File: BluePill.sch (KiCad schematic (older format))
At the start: 68 parts

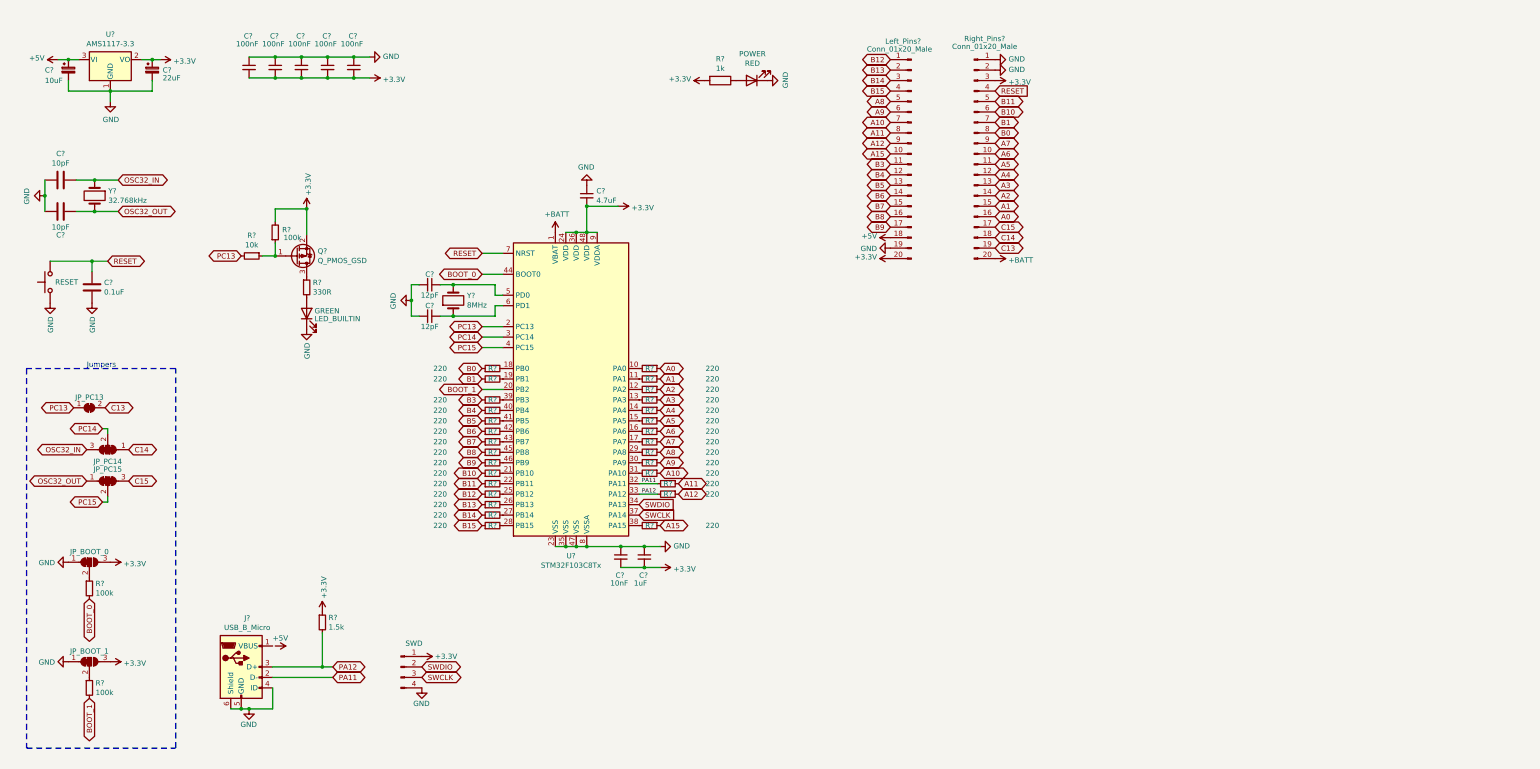
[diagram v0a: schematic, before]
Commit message: Finish schematic
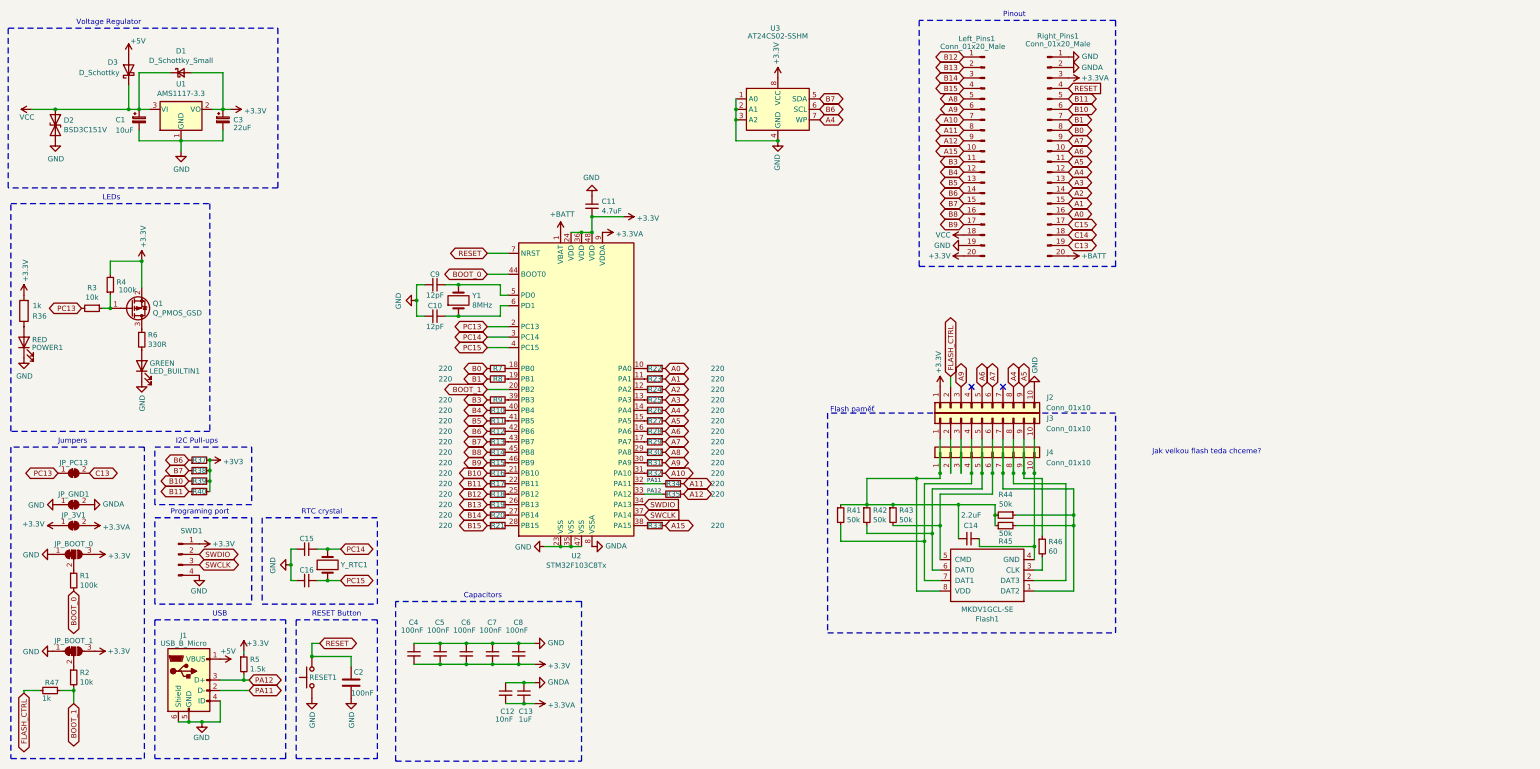
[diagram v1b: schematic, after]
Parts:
- removed C? (x2): 10pF, symbol Device:C
- removed JP_PC14, JP_PC15: SolderJumper_3_Bridged123, symbol Jumper:SolderJumper_3_Bridged123
- removed Y?: 32.768kHz, symbol Device:Crystal
- added C14: 2.2uF, Capacitor_SMD:C_0402_1005Metric, symbol Device:C_Small
- added C15, C16: ?, Capacitor_SMD:C_0603_1608Metric_Pad1.08x0.95mm_HandSolder, symbol Device:C_Small
- added D1: D_Schottky_Small, BluePill:DFN-2L_L1.0-W0.6-P0.65-RD, symbol Device:D_Schottky_Small
- added D2: BSD3C151V, Diode_SMD:D_SOD-323, symbol Device:D_TVS
- added D3: D_Schottky, Diode_SMD:D_SOD-323F, symbol Device:D_Schottky
- added Flash1: MKDV1GCL-SE, BluePill:LGA-8_L6.0-W8.0-P1.27-TL, symbol LGA-8_L6.0-W8.0-P1.27-TL:LGA-8_L6.0-W8.0-P1.27-TL
- added J2, J3, J4: Conn_01x10, symbol Connector_Generic:Conn_01x10
- added JP_3V1: 3V3, Jumper:SolderJumper-2_P1.3mm_Bridged_RoundedPad1.0x1.5mm, symbol Jumper:SolderJumper_2_Bridged
- added JP_GND1: GND, Jumper:SolderJumper-2_P1.3mm_Bridged_RoundedPad1.0x1.5mm, symbol Jumper:SolderJumper_2_Bridged
- added R37, R38, R39, R40: ?, Resistor_SMD:R_0603_1608Metric_Pad0.98x0.95mm_HandSolder, symbol Device:R_Small
- added R41, R42, R43, R44, R45: 50k, Resistor_SMD:R_0402_1005Metric, symbol Device:R_Small
- added R46: 60, Resistor_SMD:R_0402_1005Metric, symbol Device:R_Small
- added R47: 1k, Resistor_SMD:R_0402_1005Metric, symbol Device:R_Small
- added U3: AT24CS02-SSHM, Package_SO:SOIC-8_3.9x4.9mm_P1.27mm, symbol Memory_EEPROM:AT24CS02-SSHM
- added Y_RTC1: ?, Crystal:Crystal_SMD_5032-2Pin_5.0x3.2mm_HandSoldering, symbol Device:Crystal
- C1: renamed from C?; footprint (none) -> Capacitor_Tantalum_SMD:CP_EIA-3216-18_Kemet-A; LCSC (none) -> C117023
- C10, C12, C4, C5, C6, C7, C8, C9: renamed from C?; footprint (none) -> Capacitor_SMD:C_0402_1005Metric
- C11: renamed from C?; footprint (none) -> Capacitor_SMD:C_0402_1005Metric; LCSC (none) -> C23733; Note (none) -> This has to be connected near the same pin as in datasheet!
- C13: renamed from C?; footprint (none) -> Capacitor_SMD:C_0402_1005Metric; LCSC (none) -> C52923
- C2: renamed from C?; value 0.1uF -> 100nF; footprint (none) -> Capacitor_SMD:C_0402_1005Metric
- C3: renamed from C?; footprint (none) -> Capacitor_Tantalum_SMD:CP_EIA-2012-15_AVX-P; LCSC (none) -> C11383
- J1: renamed from J?; footprint (none) -> BluePill:MICRO-USB-SMD_MICRO-USB-A11; LCSC (none) -> C145783
- JP_BOOT_0, JP_BOOT_1: footprint (none) -> Jumper:SolderJumper-3_P1.3mm_Bridged12_RoundedPad1.0x1.5mm
- JP_PC13: footprint (none) -> Jumper:SolderJumper-2_P1.3mm_Bridged_RoundedPad1.0x1.5mm
- Left_Pins1: renamed from Left_Pins?; footprint (none) -> Connector_PinHeader_2.54mm:PinHeader_1x20_P2.54mm_Vertical
- Q1: renamed from Q?; footprint (none) -> BluePill:VBTA2245M; LCSC (none) -> C692958
- R1, R10, R11, R12, R13, R14, R15, R16, R17, R18, R19, R20, R21, R22, R23, R24, R25, R26, R27, R28, R29, R3, R30, R31, R32, R33, R34, R35, R36, R4, R5, R6, R7, R8, R9: renamed from R?; footprint (none) -> Resistor_SMD:R_0402_1005Metric
- R2: renamed from R?; value 100k -> 10k; footprint (none) -> Resistor_SMD:R_0402_1005Metric
- RESET1: renamed from RESET; footprint (none) -> BluePill:KEY-SMD_B3U-1000PM; LCSC (none) -> C231329
- Right_Pins1: renamed from Right_Pins?; footprint (none) -> Connector_PinHeader_2.54mm:PinHeader_1x20_P2.54mm_Vertical
- SWD1: renamed from SWD; footprint (none) -> Connector_PinHeader_2.54mm:PinHeader_1x04_P2.54mm_Vertical
- Y1: renamed from Y?; footprint (none) -> BluePill:OSC-SMD_L5.0-W3.2
- gave numbers to parts that had none: 2
- renumbered LED_BUILTIN to LED_BUILTIN1, POWER to POWER1
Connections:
- net +3V3: now also D1.2 (A), J2.1 (Pin_1), JP_3V1.1 (A), R37.2, R38.2, R39.2, R40.2, U3.8 (VCC); no longer C12.2, C13.2, Right_Pins1.3 (Pin_3), U2.9 (VDDA)
- net +5V: now also J1.1 (VBUS), D3.2 (A); no longer C1.1, Left_Pins1.18 (Pin_18), U1.3 (VI)
- net A4: now also J2.8 (Pin_8), U3.7 (WP)
- net A5: now also J2.9 (Pin_9)
- net A6: now also J2.5 (Pin_5)
- net A7: now also J2.6 (Pin_6)
- net A9: now also J2.3 (Pin_3)
- net B10: now also R39.1
- net B11: now also R40.1
- net B6: now also R37.1, U3.6 (SCL)
- net B7: now also R38.1, U3.5 (SDA)
- net BOOT_1: now also R47.1
- net GND: now also C15.2, C16.2, D2.2 (A2), J2.10 (Pin_10), JP_GND1.1 (A), U3.1 (A0), U3.2 (A1), U3.3 (A2), U3.4 (GND); no longer C12.1, C13.1, Right_Pins1.2 (Pin_2), U2.8 (VSSA)
- net PC14: now also C15.1, Y_RTC1.2
- net PC15: now also C16.1, Y_RTC1.1
- new net: C14.2, Flash1.8 (VDD), J3.1 (Pin_1), J4.1 (Pin_1), R41.1, R42.1, R43.1, R44.2, R45.1
- new net: C14.1, Flash1.4 (GND), J3.10 (Pin_10), J4.10 (Pin_10)
- new net: J3.2 (Pin_2), J4.2 (Pin_2)
- new net: J3.3 (Pin_3), J4.3 (Pin_3)
- new net: Flash1.7 (DAT1), J3.4 (Pin_4), J4.4 (Pin_4), R41.2
- new net: Flash1.6 (DAT0), J3.5 (Pin_5), J4.5 (Pin_5), R42.2
- new net: Flash1.5 (CMD), J3.6 (Pin_6), J4.6 (Pin_6), R43.2
- new net: Flash1.1 (DAT2), J3.7 (Pin_7), J4.7 (Pin_7), R44.1, R45.2
- new net: Flash1.2 (DAT3), J3.8 (Pin_8), J4.8 (Pin_8)
- new net: J3.9 (Pin_9), J4.9 (Pin_9), R46.1
- new net: Flash1.3 (CLK), R46.2
- new net +3.3VA: C12.2, C13.2, JP_3V1.2 (B), Right_Pins1.3 (Pin_3), U2.9 (VDDA)
- new net FLASH_CTRL: J2.2 (Pin_2), R47.2
- new net GNDA: C12.1, C13.1, JP_GND1.2 (B), Right_Pins1.2 (Pin_2), U2.8 (VSSA)
- new net VCC: C1.1, D1.1 (K), D2.1 (A1), D3.1 (K), Left_Pins1.18 (Pin_18), U1.3 (VI)
- no-connect marks 0 -> 2
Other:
- note added: "Capacitors"
- note added: "Flash paměť"
- note added: "I2C Pull-ups"
- note added: "Jak velkou flash teda chceme?"
- note added: "LEDs"
- note added: "Pinout"
- note added: "Programing port"
- note added: "RESET Button"
- note added: "RTC crystal"
- note added: "USB"
- note added: "Voltage Regulator"
- moved on the sheet: C1, C10, C11, C12, C13, C2, C3, C4, C5, C6, C7, C8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

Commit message: Add LCSC numbers
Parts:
- C12: LCSC (none) -> C15195
- C2, C4, C5, C6, C7, C8: LCSC (none) -> C1525
- R1, R4: LCSC (none) -> C25741
- R10, R11, R12, R13, R14, R15, R16, R17, R18, R19, R20, R21, R22, R23, R24, R25, R26, R27, R28, R29, R30, R31, R32, R33, R34, R35, R7, R8, R9: LCSC (none) -> C25091
- R2, R3: LCSC (none) -> C25744
- R36, R47: LCSC (none) -> C11702
- R41, R42, R43, R44, R45: value 50k -> 51k; LCSC (none) -> C25794
- R46: value 60 -> 51; LCSC (none) -> C25125
- R5: LCSC (none) -> C25867
- R6: LCSC (none) -> C25104
- U1: LCSC (none) -> C6186
- U2: LCSC (none) -> C8734
- Y_RTC1: LCSC C156253 -> (none)

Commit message: Route board
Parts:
- removed C14: 2.2uF, Capacitor_SMD:C_0402_1005Metric, symbol Device:C_Small
- removed Flash1: MKDV1GCL-SE, BluePill:LGA-8_L6.0-W8.0-P1.27-TL, symbol LGA-8_L6.0-W8.0-P1.27-TL:LGA-8_L6.0-W8.0-P1.27-TL
- removed J1: USB_B_Micro, BluePill:MICRO-USB-SMD_MICRO-USB-A11, symbol Connector:USB_B_Micro
- removed J3, J4: Conn_01x10, symbol Connector_Generic:Conn_01x10
- removed R12, R13, R14, R15, R16, R17, R18, R19, R20, R21, R22, R23, R24, R25, R26, R27, R28, R29, R30, R31, R32, R34, R7, R8: 220, Resistor_SMD:R_0402_1005Metric, symbol Device:R_Small
- removed R41, R42, R43, R44, R45: 51k, Resistor_SMD:R_0402_1005Metric, symbol Device:R_Small
- removed R46: 51, Resistor_SMD:R_0402_1005Metric, symbol Device:R_Small
- added ADDR1, ADDR2, ADDR3: GND, Jumper:SolderJumper-2_P1.3mm_Bridged_RoundedPad1.0x1.5mm, symbol Jumper:SolderJumper_2_Bridged
- added J5: USB_B_Micro, BluePill:MICRO-USB-SMD_MICRO-USB-A11, symbol Connector:USB_B_Micro
- added RN1, RN2, RN3, RN4, RN5, RN6: 4x220, Resistor_SMD:R_Array_Concave_4x0402, symbol Device:R_Pack04
- D1: renamed from D2; footprint Diode_SMD:D_SOD-323 -> Resistor_SMD:R_1206_3216Metric_Pad1.30x1.75mm_HandSolder
- J1: renamed from J2; footprint (none) -> BluePill:Flash_connector
- R3: renamed from R1; value 100k -> 10k; LCSC C25741 -> C25744
- SWD1: footprint Connector_PinHeader_2.54mm:PinHeader_1x04_P2.54mm_Vertical -> Connector_Harwin:Harwin_M20-89004xx_1x04_P2.54mm_Horizontal
- renumbered C6 to C10, C7 to C11, C8 to C13, C13 to C14, C11 to C15, C3 to C2, C15 to C3, C16 to C4, C2 to C5, C4 to C6, C9 to C7, C10 to C8, C5 to C9, D3 to D2, D1 to D3, JP_BOOT_0 to JP_BOOT_1, JP_BOOT_1 to JP_BOOT_2, JP_PC13 to JP_PC1, R36 to R1, R39 to R10, R40 to R11, R5 to R12, R9 to R13, R10 to R14, R11 to R15, R33 to R16, R35 to R17, R47 to R2, R2 to R4, R3 to R5, R4 to R6, R6 to R7, R37 to R8, R38 to R9
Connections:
- net C14 is gone; now on net PC14: Right_Pins1.18 (Pin_18)
- net C15 is gone; now on net PC15: Right_Pins1.17 (Pin_17)
- net +3V3: now also SWD1.4 (Pin_4); no longer SWD1.1 (Pin_1)
- net +5V: now also J5.1 (VBUS)
- net A0: now also RN4.1 (R1.1)
- net A1: now also RN4.2 (R2.1)
- net A10: now also RN6.7 (R2.2)
- net A11: now also RN6.8 (R1.2)
- net A2: now also RN4.3 (R3.1)
- net A3: now also RN4.4 (R4.1)
- net A4: now also RN5.5 (R4.2)
- net A5: now also RN5.6 (R3.2)
- net A6: now also RN5.7 (R2.2)
- net A7: now also RN5.8 (R1.2)
- net A8: now also RN6.5 (R4.2)
- net A9: now also RN6.6 (R3.2)
- net B0: now also RN1.1 (R1.1)
- net B1: now also RN1.2 (R2.1)
- net B10: now also RN1.3 (R3.1)
- net B11: now also RN1.4 (R4.1)
- net B12: now also RN3.1 (R1.1)
- net B13: now also RN3.2 (R2.1)
- net B14: now also RN3.3 (R3.1)
- net B15: now also RN3.4 (R4.1)
- net B6: now also RN2.1 (R1.1)
- net B7: now also RN2.2 (R2.1)
- net B8: now also RN2.3 (R3.1)
- net B9: now also RN2.4 (R4.1)
- net GND: now also SWD1.1 (Pin_1), ADDR1.1 (A), ADDR2.1 (A), ADDR3.1 (A), J5.4 (ID), J5.5 (GND), J5.6 (Shield); no longer SWD1.4 (Pin_4), U3.1 (A0), U3.2 (A1), U3.3 (A2)
- net PA11: now also J5.2 (D-), RN6.1 (R1.1)
- net PA12: now also J5.3 (D+)
- net SWCLK: now also SWD1.2 (Pin_2); no longer SWD1.3 (Pin_3)
- net SWDIO: now also SWD1.3 (Pin_3); no longer SWD1.2 (Pin_2)
- net at U2.10 (PA0): now also RN4.8 (R1.2)
- net at U2.11 (PA1): now also RN4.7 (R2.2)
- net at U2.12 (PA2): now also RN4.6 (R3.2)
- net at U2.13 (PA3): now also RN4.5 (R4.2)
- net at U2.14 (PA4): now also RN5.4 (R4.1)
- net at U2.15 (PA5): now also RN5.3 (R3.1)
- net at U2.16 (PA6): now also RN5.2 (R2.1)
- net at U2.17 (PA7): now also RN5.1 (R1.1)
- net at U2.18 (PB0): now also RN1.8 (R1.2)
- net at U2.19 (PB1): now also RN1.7 (R2.2)
- net at U2.21 (PB10): now also RN1.6 (R3.2)
- net at U2.22 (PB11): now also RN1.5 (R4.2)
- net at U2.25 (PB12): now also RN3.8 (R1.2)
- net at U2.26 (PB13): now also RN3.7 (R2.2)
- net at U2.27 (PB14): now also RN3.6 (R3.2)
- net at U2.28 (PB15): now also RN3.5 (R4.2)
- net at U2.29 (PA8): now also RN6.4 (R4.1)
- net at U2.30 (PA9): now also RN6.3 (R3.1)
- net at U2.31 (PA10): now also RN6.2 (R2.1)
- net at U2.42 (PB6): now also RN2.8 (R1.2)
- net at U2.43 (PB7): now also RN2.7 (R2.2)
- net at U2.45 (PB8): now also RN2.6 (R3.2)
- net at U2.46 (PB9): now also RN2.5 (R4.2)
- new net: ADDR1.2 (B), U3.1 (A0)
- new net: ADDR2.2 (B), U3.2 (A1)
- new net: ADDR3.2 (B), U3.3 (A2)
